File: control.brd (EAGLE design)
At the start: 100 x 80 mm, 110 parts, among them IC1 LM358N, IC2 XMEGA16A4A, IC3 LM317MBSTT3, IC5 LM358N, Q1 BSS123, Q10 TIP42C, Q11 BC338, Q12 BC548, Q13 BC557C, Q14 BSS123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

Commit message: LEDs
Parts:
- added LED1, LED2, LED3, LED4: (no value), led:CHIPLED_0805
- added R19, R20, R62, R63: 33k, resistor:M0805
- moved C1 2.54 mm to (36.2, 36.8)
- moved C6 2.54 mm to (44.5, 29.8)
- moved C9 2.54 mm to (40.0, 29.8)
- moved IC3 1.80 mm to (41.9, 35.6)
- moved JP1 1.27 mm to (35.6, 47.0)
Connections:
- new net N$10: IC2.21, R20.1
- new net N$39: IC2.22, R62.1
- new net N$5: IC2.20, R19.1
- new net N$58: IC2.23, R63.1
- new net N$59: LED4.A, R63.2
- new net N$60: LED3.A, R62.2
- new net N$61: LED2.A, R20.2
- new net N$62: LED1.A, R19.2
- net GND: now also LED1.C, LED2.C, LED3.C, LED4.C
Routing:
- net N$60: track 0.00 -> 7.89 mm, vias 0 -> 1
- net N$59: track 0.00 -> 7.44 mm, vias 0 -> 1
- net N$5: track 0.00 -> 5.90 mm, vias 0 -> 1
- net N$62: track 0.00 -> 5.59 mm
- net N$10: track 0.00 -> 3.93 mm, vias 0 -> 1
- net GND: track 66.5 -> 69.0 mm
- net N$61: track 0.00 -> 2.52 mm
- net N$39: track 0.00 -> 2.08 mm
- net N$58: track 0.00 -> 1.94 mm
- net +12V: track 161.2 -> 163.0 mm
- net N$38: track 5.86 -> 7.50 mm
- net EN_B1: track 35.1 -> 36.6 mm
- net N$27: track 5.14 -> 5.66 mm

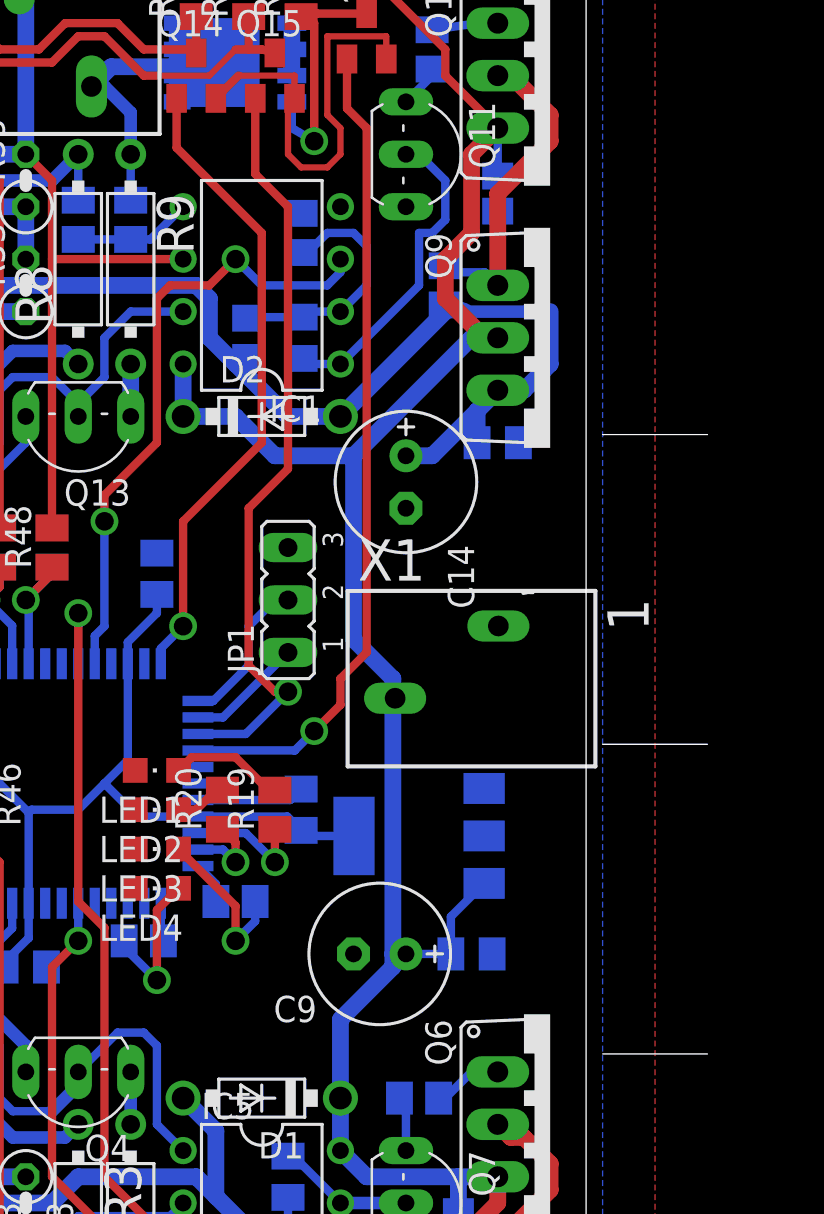
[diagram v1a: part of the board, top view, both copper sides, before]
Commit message: power connector hohlstecker
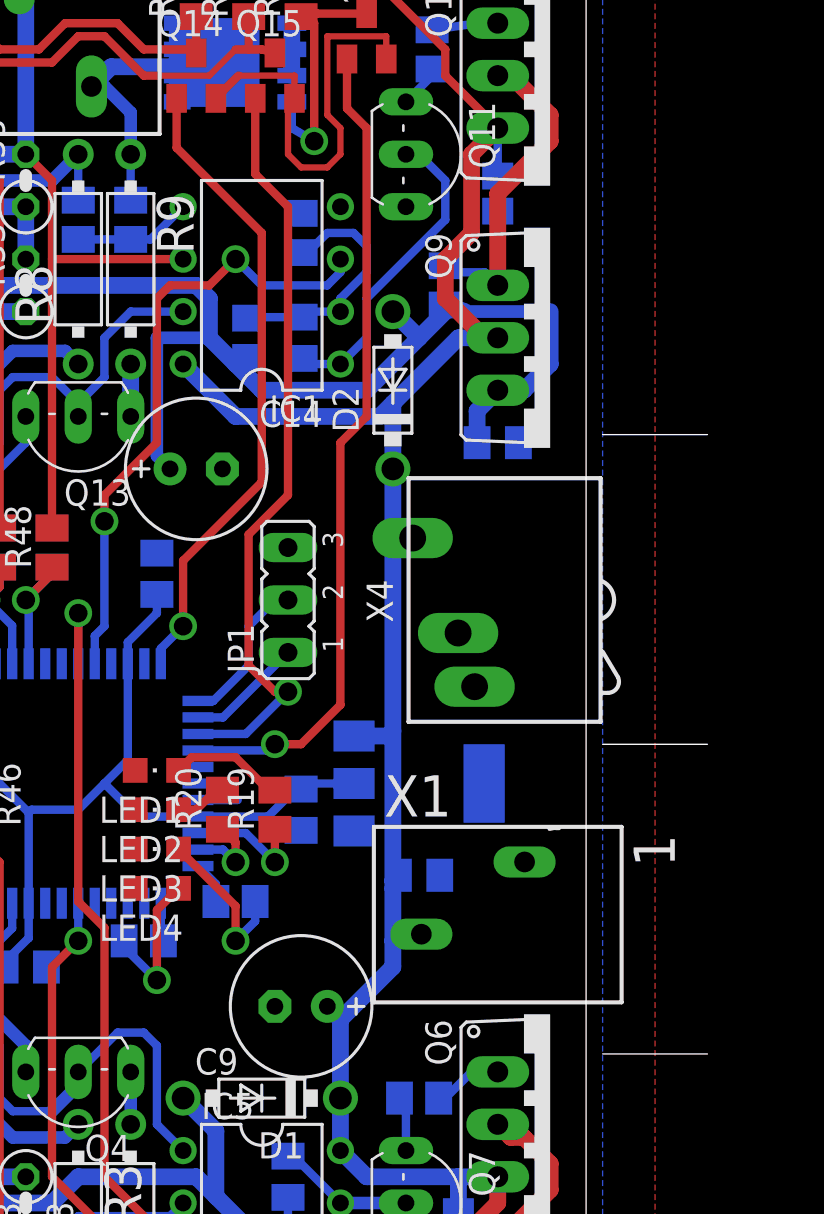
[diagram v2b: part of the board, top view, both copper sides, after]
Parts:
- added X4: NEBJ21R, con-lumberg:NEBJ21R
- IC3: value LM317MBSTT3 -> LM317MTT3-A
- moved X1 11.5 mm to (45.7, 31.8)
- moved C14 10.2 mm to (31.1, 53.3), turned to 0 degrees
- moved D2 6.48 mm to (40.6, 57.1), turned to 90 degrees
- moved C6 4.58 mm to (41.9, 33.7)
- moved C9 4.58 mm to (36.2, 27.3)
- moved IC3 2.54 mm to (41.9, 38.1), turned to 90 degrees
- turned C1 to 270 degrees
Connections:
- net +12V: now also X4.1
- net +3V3: now also IC3.2; no longer IC3.4
- net GND: now also X4.3
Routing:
- net ADC8: track 71.4 -> 76.9 mm
- net GND: track 69.0 -> 65.8 mm
- net +12V: track 163.0 -> 160.6 mm

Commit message: gnd vias
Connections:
- net GND: now also X4.2
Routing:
- net GND: vias 0 -> 3
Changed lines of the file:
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@@
 <contactref element="LED4" pad="C"/>
 <contactref element="X4" pad="3"/>
+<contactref element="X4" pad="2"/>
+<via x="31.75" y="44.45" extent="1-16" drill="0.9" shape="octagon"/>
+<via x="38.1" y="33.02" extent="1-16" drill="0.9" shape="octagon"/>
+<via x="46.99" y="38.1" extent="1-16" drill="0.9" shape="octagon"/>
 </signal>
 <signal name="+12V">

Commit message: transistor to bc548
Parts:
- Q11, Q7: value BC338 -> BC548
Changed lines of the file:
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@@
 <element name="Q5" library="transistor-power" package="TO220AV" value="TIP41C" x="48.26" y="8.89" rot="R270"/>
 <element name="Q6" library="transistor-power" package="TO220AV" value="TIP42C" x="48.26" y="21.59" rot="R270"/>
-<element name="Q7" library="transistor-npn" package="TO92-EBC" value="BC338" x="42.545" y="17.78" rot="R270"/>
+<element name="Q7" library="transistor-npn" package="TO92-EBC" value="BC548" x="42.545" y="17.78" rot="R270"/>
 <element name="R24" library="resistor" package="0207/2V" value="1" x="12.7" y="12.7" rot="R90"/>
 <element name="R25" library="resistor" package="0207/2V" value="1" x="13.97" y="16.51" rot="R180"/>
@@
 <element name="Q9" library="transistor-power" package="TO220AV" value="TIP41C" x="48.26" y="59.69" rot="R270"/>
 <element name="Q10" library="transistor-power" package="TO220AV" value="TIP42C" x="48.26" y="72.39" rot="R270"/>
-<element name="Q11" library="transistor-npn" package="TO92-EBC" value="BC338" x="42.545" y="68.58" rot="R270"/>
+<element name="Q11" library="transistor-npn" package="TO92-EBC" value="BC548" x="42.545" y="68.58" rot="R270"/>
 <element name="R49" library="resistor" package="0207/2V" value="1" x="12.7" y="63.5" rot="R270"/>
 <element name="R50" library="resistor" package="0207/2V" value="1" x="15.24" y="63.5" rot="R270"/>
